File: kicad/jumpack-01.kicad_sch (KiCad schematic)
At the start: 13 parts, among them J1 GPIO, J2 Screw_Terminal_01x03, J3 Conn_01x04, J4 Conn_01x08, J5 Conn_01x04, J6 Source, J7 Load

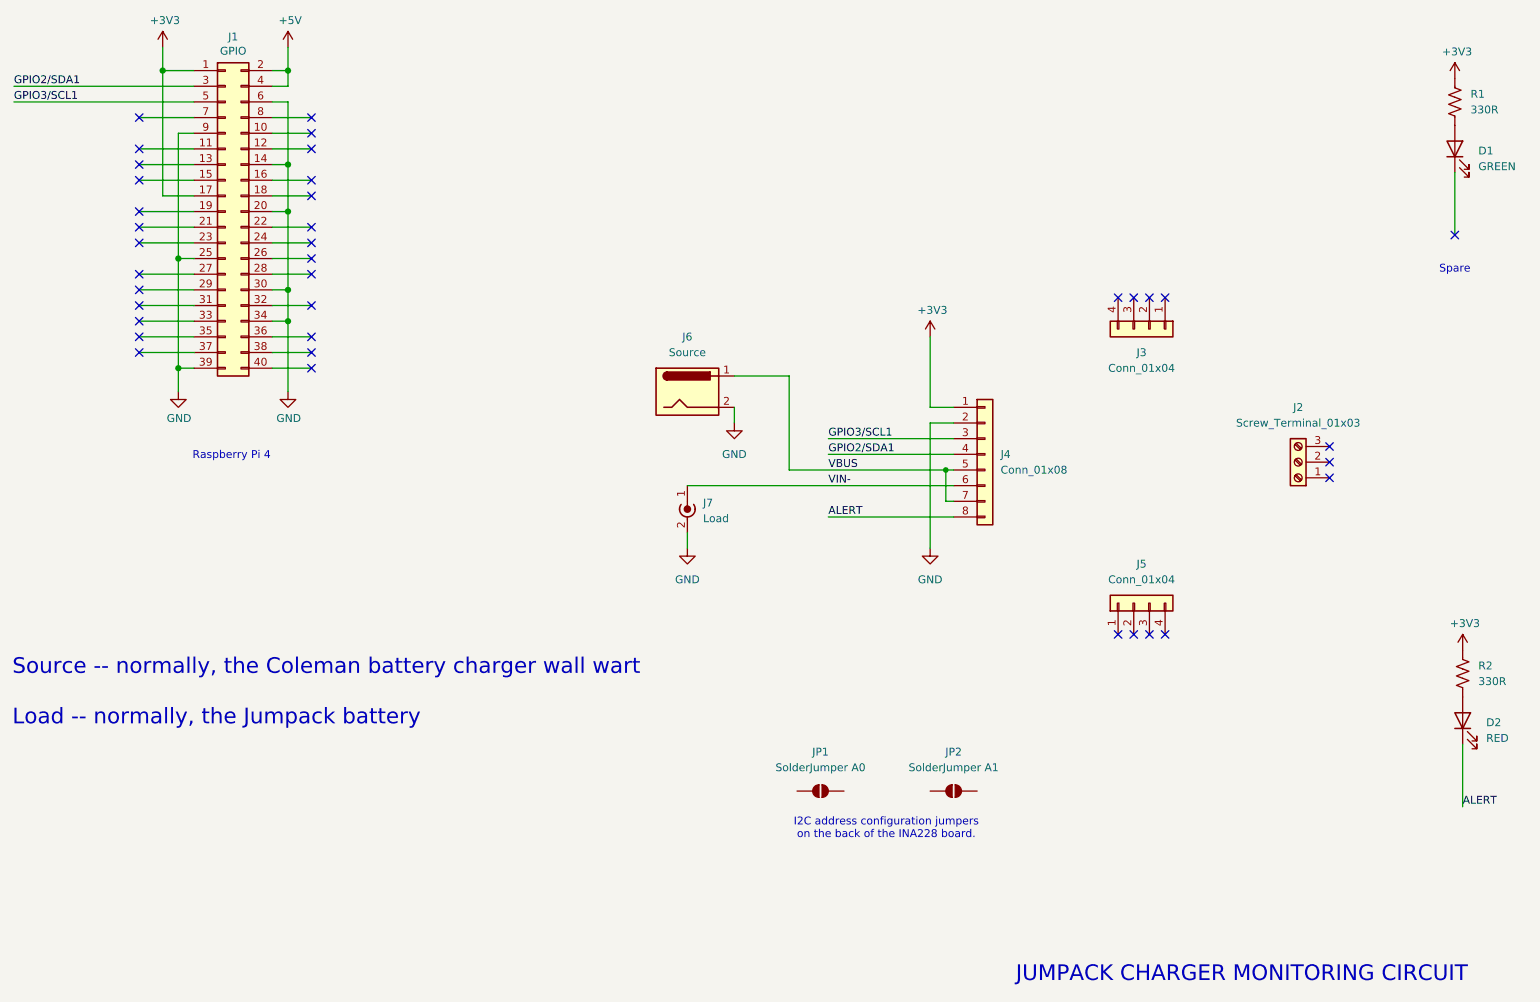
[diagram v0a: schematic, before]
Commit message: initial draft of logger-v3; update docs, wiring
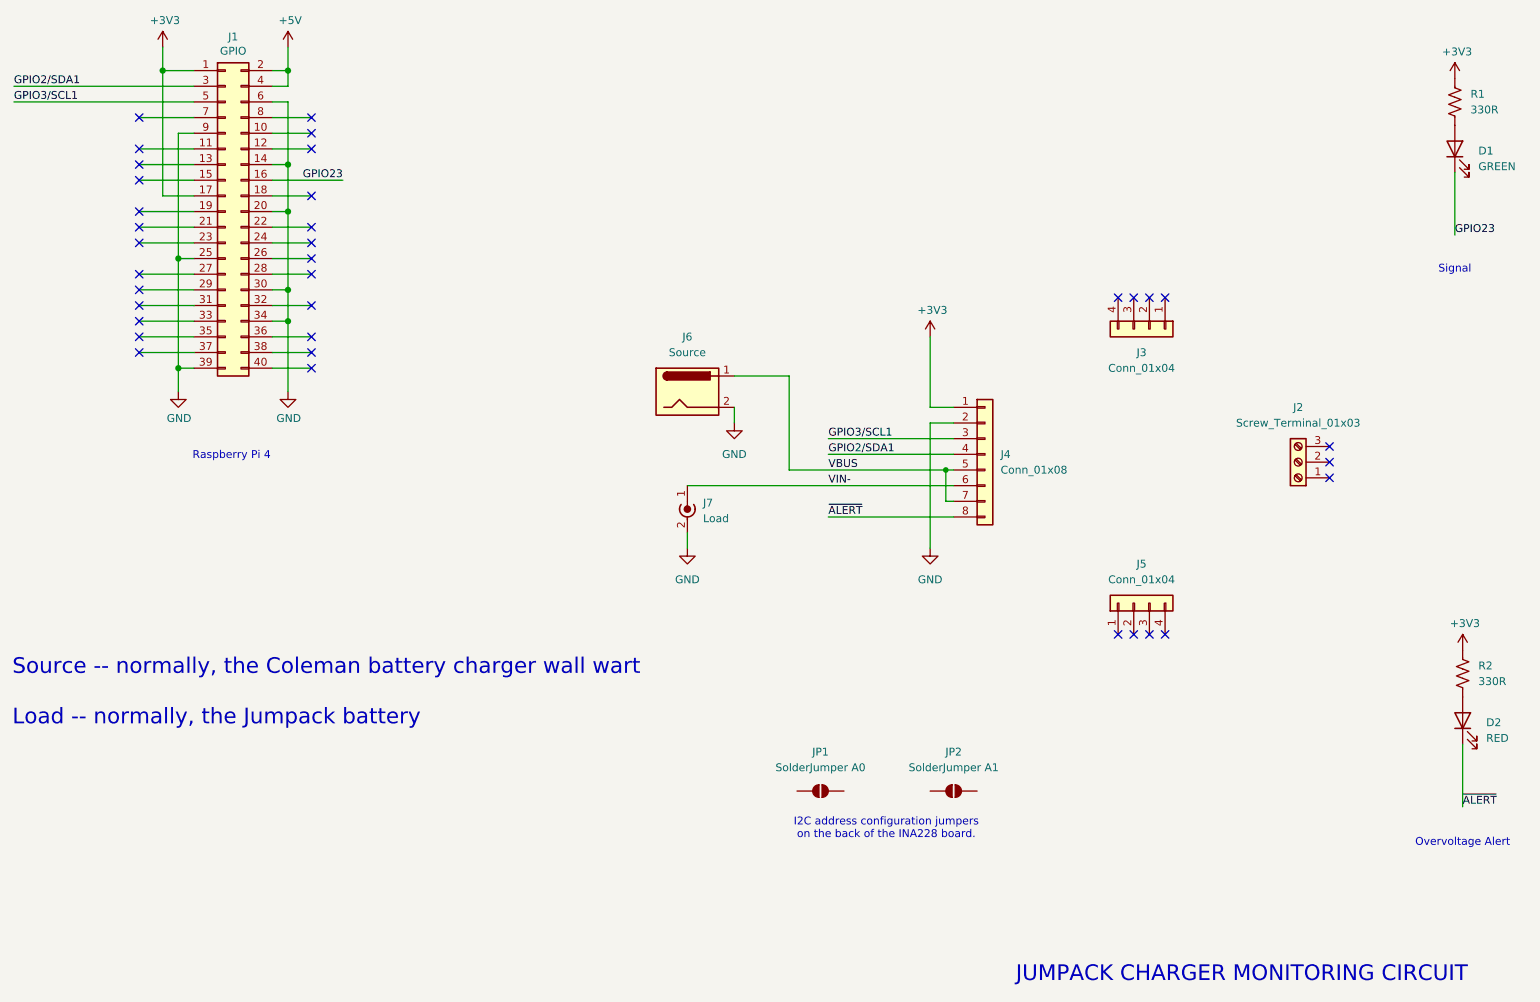
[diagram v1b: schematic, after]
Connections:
- net GPIO23: now reaches J1.16 (Pin_16)
- net GPIO23: now also D1.1 (K)
- net ALERT renamed ~{ALERT}
- no-connect marks 38 -> 36
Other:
- note added: "Overvoltage Alert"
- note added: "Signal"
- note removed: "Spare"
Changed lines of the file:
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@@
 		)
 	)
-	(text "Spare"
+	(text "Signal"
 		(exclude_from_sim no)
 		(at 265.43 60.198 0)
@@
 		)
 	)
+	(text "Overvoltage Alert"
+		(exclude_from_sim no)
+		(at 266.7 153.162 0)
+		(effects
+			(font
+				(size 1.27 1.27)
+			)
+		)
+	)
 	(junction
 		(at 76.2 27.94)
@@
 	)
 	(no_connect
-		(at 265.43 54.61)
-	)
-	(no_connect
 		(at 80.01 58.42)
 	)
@@
 	)
 	(no_connect
-		(at 80.01 45.72)
-	)
-	(no_connect
 		(at 245.11 91.44)
 	)
@@
 	(wire
 		(pts
-			(xy 73.66 45.72) (xy 80.01 45.72)
+			(xy 73.66 45.72) (xy 85.09 45.72)
 		)
 		(stroke
@@
 		)
 	)
+	(label "GPIO23"
+		(at 85.09 45.72 180)
+		(effects
+			(font
+				(size 1.27 1.27)
+			)
+			(justify right bottom)
+		)
+	)
 	(label "GPIO3{slash}SCL1"
 		(at 163.83 87.63 0)
@@
 		)
 	)
-	(label "ALERT"
+	(label "~{ALERT}"
 		(at 266.7 147.32 0)
 		(effects
@@
 		)
 	)
-	(label "ALERT"
+	(label "GPIO23"
+		(at 265.43 54.61 0)
+		(effects
+			(font
+				(size 1.27 1.27)
+			)
+			(justify left bottom)
+		)
+	)
+	(label "~{ALERT}"
 		(at 163.83 100.33 0)
 		(effects
